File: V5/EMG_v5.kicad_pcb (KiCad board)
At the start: 2 copper layers, 75.2 x 32 mm, 20 parts, among them J1 SJ1-3523N, J2 Output, U1 INA333xxDGK, U2 MCP6002-xP

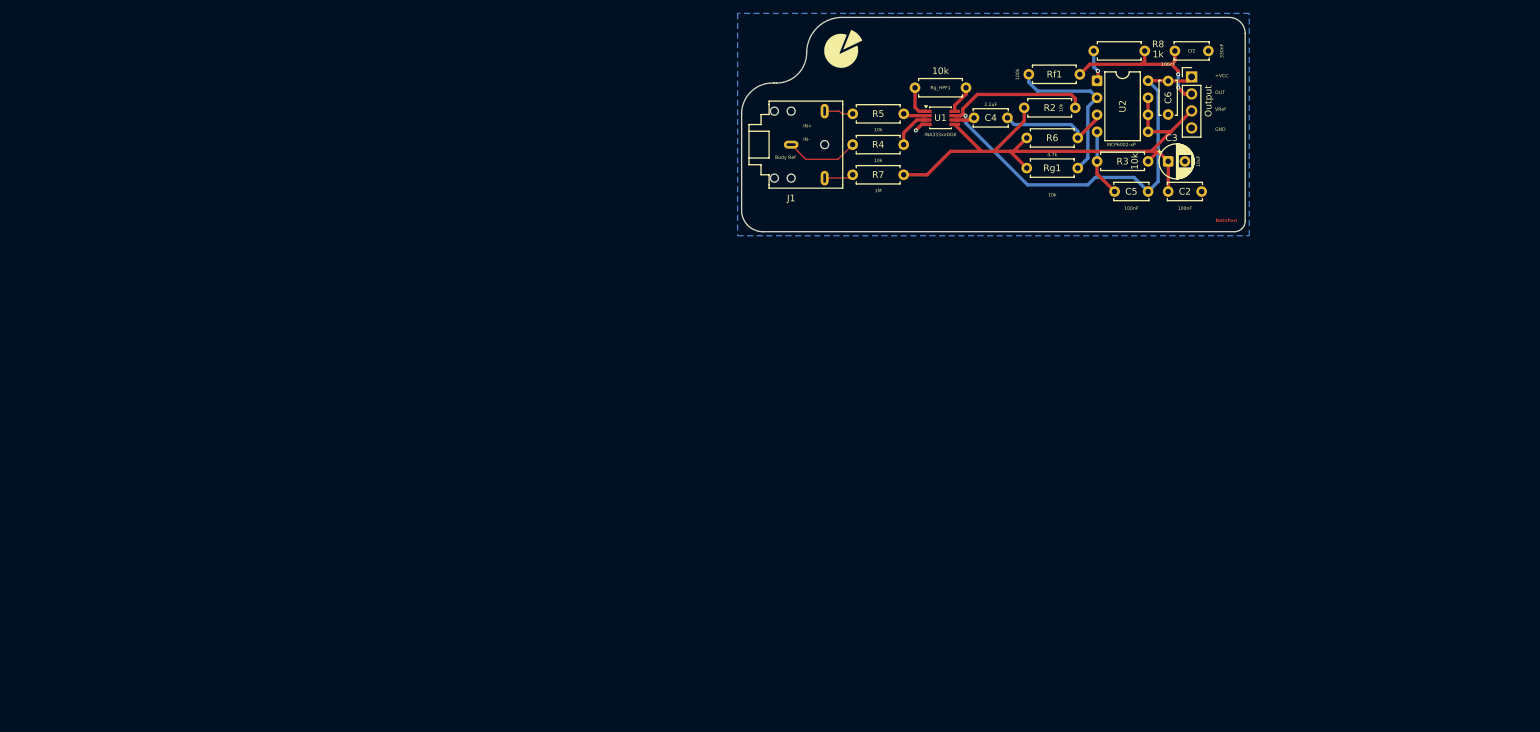
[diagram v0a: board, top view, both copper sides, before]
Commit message: Place EMG V5 PCB blocks and fix analog feedback nets
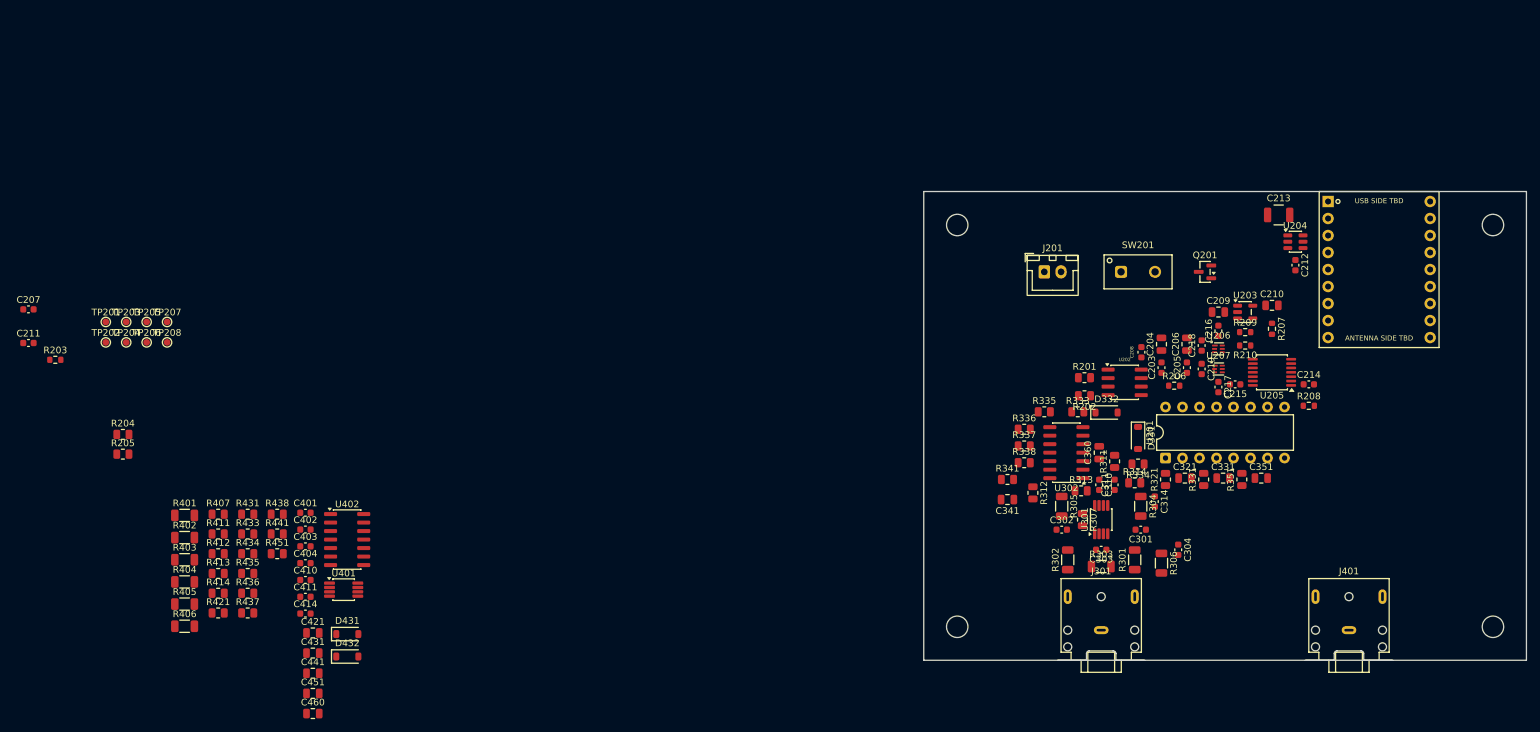
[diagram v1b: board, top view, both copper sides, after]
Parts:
- removed C2, C5, C6: 100nF, Capacitor_THT:C_Disc_D5.0mm_W2.5mm_P5.00mm
- removed C3: 10uF, Capacitor_THT:CP_Radial_D5.0mm_P2.50mm
- removed C4: 2.2uF, Capacitor_THT:C_Disc_D5.0mm_W2.5mm_P5.00mm
- removed Cf2: 330nF, Capacitor_THT:C_Disc_D5.0mm_W2.5mm_P5.00mm
- removed J1: SJ1-3523N, Connector_Audio:Jack_3.5mm_CUI_SJ1-3523N_Horizontal
- removed J2: Output, Connector_PinHeader_2.54mm:PinHeader_1x04_P2.54mm_Vertical
- removed R2, R3, R4, R5, Rg1, Rg_HPF1: 10k, Resistor_THT:R_Axial_DIN0207_L6.3mm_D2.5mm_P7.62mm_Horizontal
- removed R6: 4.7k, Resistor_THT:R_Axial_DIN0207_L6.3mm_D2.5mm_P7.62mm_Horizontal
- removed R7: 1M, Resistor_THT:R_Axial_DIN0207_L6.3mm_D2.5mm_P7.62mm_Horizontal
- removed R8: 1k, Resistor_THT:R_Axial_DIN0207_L6.3mm_D2.5mm_P7.62mm_Horizontal
- removed Rf1: 100k, Resistor_THT:R_Axial_DIN0207_L6.3mm_D2.5mm_P7.62mm_Horizontal
- removed U1: INA333xxDGK, Package_SO:VSSOP-8_3x3mm_P0.65mm
- removed U2: MCP6002-xP, Package_DIP:DIP-8_W7.62mm
- added C203: 100nF, Capacitor_SMD:C_0603_1608Metric, F.Cu at (75.5, 66.3)
- added C204: 1uF, Capacitor_SMD:C_0805_2012Metric, F.Cu at (75.5, 62.8)
- added C205: 100nF, Capacitor_SMD:C_0603_1608Metric, F.Cu at (79.3, 66.3)
- added C206: 1uF, Capacitor_SMD:C_0805_2012Metric, F.Cu at (79.3, 62.8)
- added C207: 220pF, Capacitor_SMD:C_0603_1608Metric, F.Cu at (-93.7, 57.6)
- added C208: 100nF, Capacitor_SMD:C_0603_1608Metric, F.Cu at (72.5, 64.0)
- added C209: 2.2uF, Capacitor_SMD:C_0805_2012Metric, F.Cu at (84.0, 58.0)
- added C210: 2.2uF, Capacitor_SMD:C_0805_2012Metric, F.Cu at (92.0, 57.0)
- added C211: 10nF, Capacitor_SMD:C_0603_1608Metric, F.Cu at (-93.7, 62.6)
- added C212: 2.2nF, Capacitor_SMD:C_0603_1608Metric, F.Cu at (95.5, 51.0)
- added C213: 47uF, EMG_V5:C_1210_3225_Murata_GRM32_Reflow, F.Cu at (93.0, 43.5)
- added C214: 100nF, Capacitor_SMD:C_0603_1608Metric, F.Cu at (97.5, 68.8)
- added C215: 100nF, Capacitor_SMD:C_0603_1608Metric, F.Cu at (86.5, 68.8)
- added C216: 100nF, Capacitor_SMD:C_0603_1608Metric, F.Cu at (84.0, 60.8)
- added C217: 100nF, Capacitor_SMD:C_0603_1608Metric, F.Cu at (84.0, 69.2)
- added C218: 9.1nF, Capacitor_SMD:C_0603_1608Metric, F.Cu at (81.5, 63.0)
- added C219: 9.1nF, Capacitor_SMD:C_0603_1608Metric, F.Cu at (81.5, 66.5)
- added C301: 100pF, Capacitor_SMD:C_0603_1608Metric, F.Cu at (72.4, 90.5)
- added C302: 100pF, Capacitor_SMD:C_0603_1608Metric, F.Cu at (60.6, 90.5)
- added C303: 470pF, Capacitor_SMD:C_0603_1608Metric, F.Cu at (66.5, 93.5)
- added C304: 100pF DNP, Capacitor_SMD:C_0603_1608Metric, F.Cu at (78.0, 93.5)
- added C310: 100nF, Capacitor_SMD:C_0603_1608Metric, F.Cu at (66.2, 83.8)
- added C311: 100nF, Capacitor_SMD:C_0603_1608Metric, F.Cu at (68.5, 83.8)
- added C314: 10nF, Capacitor_SMD:C_0603_1608Metric, F.Cu at (74.5, 86.3)
- added C321: 1nF, Capacitor_SMD:C_0805_2012Metric, F.Cu at (79.0, 82.8)
- added C331: 1nF, Capacitor_SMD:C_0805_2012Metric, F.Cu at (84.7, 82.8)
- added C341: 1uF, Capacitor_SMD:C_0805_2012Metric, F.Cu at (52.5, 86.0)
- added C351: 4.7nF, Capacitor_SMD:C_0805_2012Metric, F.Cu at (90.4, 82.8)
- added C360: 100nF, Capacitor_SMD:C_0805_2012Metric, F.Cu at (66.2, 79.0)
- added C401: 100pF, Capacitor_SMD:C_0603_1608Metric, F.Cu at (-52.3, 88.0)
- added C402: 100pF, Capacitor_SMD:C_0603_1608Metric, F.Cu at (-52.3, 90.5)
- added C403: 470pF, Capacitor_SMD:C_0603_1608Metric, F.Cu at (-52.3, 93.0)
- added C404: 100pF DNP, Capacitor_SMD:C_0603_1608Metric, F.Cu at (-52.3, 95.5)
- added C410: 100nF, Capacitor_SMD:C_0603_1608Metric, F.Cu at (-52.3, 98.0)
- added C411: 100nF, Capacitor_SMD:C_0603_1608Metric, F.Cu at (-52.3, 100.5)
- added C414: 10nF, Capacitor_SMD:C_0603_1608Metric, F.Cu at (-52.3, 103.0)
- added C421: 1nF, Capacitor_SMD:C_0805_2012Metric, F.Cu at (-51.2, 105.9)
- added C431: 1nF, Capacitor_SMD:C_0805_2012Metric, F.Cu at (-51.2, 108.9)
- added C441: 1uF, Capacitor_SMD:C_0805_2012Metric, F.Cu at (-51.2, 111.9)
- added C451: 4.7nF, Capacitor_SMD:C_0805_2012Metric, F.Cu at (-51.2, 115.0)
- added C460: 100nF, Capacitor_SMD:C_0805_2012Metric, F.Cu at (-51.2, 118.0)
- added D331: BAS70ZFILM, Diode_SMD:D_SOD-123, F.Cu at (72.0, 76.8)
- added D332: BAS70ZFILM, Diode_SMD:D_SOD-123, F.Cu at (67.3, 73.0)
- added D431: BAS70ZFILM, Diode_SMD:D_SOD-123, F.Cu at (-46.1, 106.1)
- added D432: BAS70ZFILM, Diode_SMD:D_SOD-123, F.Cu at (-46.1, 109.4)
- added J201: B2B-XH-A(LF)(SN), Connector_JST:JST_XH_B2B-XH-A_1x02_P2.50mm_Vertical, F.Cu at (58.0, 52.0)
- added J301: SJ1-3523N, Connector_Audio:Jack_3.5mm_CUI_SJ1-3523N_Horizontal, F.Cu at (66.5, 105.5)
- added J401: SJ1-3523N, Connector_Audio:Jack_3.5mm_CUI_SJ1-3523N_Horizontal, F.Cu at (103.5, 105.5)
- added Q201: PMV48XP, Package_TO_SOT_SMD:SOT-23, F.Cu at (82.0, 52.0)
- added R201: 47k, Resistor_SMD:R_0805_2012Metric, F.Cu at (64.0, 67.8)
- added R202: 47k, Resistor_SMD:R_0805_2012Metric, F.Cu at (64.0, 70.5)
- added R203: 1k, Resistor_SMD:R_0603_1608Metric, F.Cu at (-89.7, 65.1)
- added R204: 68k, Resistor_SMD:R_0805_2012Metric, F.Cu at (-79.6, 76.3)
- added R205: 100k, Resistor_SMD:R_0805_2012Metric, F.Cu at (-79.6, 79.2)
- added R206: 0R, Resistor_SMD:R_0603_1608Metric, F.Cu at (77.4, 69.0)
- added R207: 0R, Resistor_SMD:R_0603_1608Metric, F.Cu at (92.0, 60.5)
- added R208: 10k, Resistor_SMD:R_0603_1608Metric, F.Cu at (97.5, 72.0)
- added R209: 47k 1%, Resistor_SMD:R_0603_1608Metric, F.Cu at (88.0, 61.0)
- added R210: 220k 1%, Resistor_SMD:R_0603_1608Metric, F.Cu at (88.0, 63.0)
- added R301: 100k, Resistor_SMD:R_1206_3216Metric, F.Cu at (71.5, 95.0)
- added R302: 100k, Resistor_SMD:R_1206_3216Metric, F.Cu at (61.5, 95.0)
- added R303: 220k, Resistor_SMD:R_1206_3216Metric, F.Cu at (66.5, 96.0)
- added R304: 10M, Resistor_SMD:R_1206_3216Metric, F.Cu at (72.4, 87.0)
- added R305: 10M, Resistor_SMD:R_1206_3216Metric, F.Cu at (60.6, 87.0)
- added R306: 2.2M, Resistor_SMD:R_1206_3216Metric, F.Cu at (75.5, 95.5)
- added R307: 4.99k 0.1% RG, Resistor_SMD:R_0805_2012Metric, F.Cu at (63.7, 89.0)
- added R311: 100k, Resistor_SMD:R_0805_2012Metric, F.Cu at (68.5, 80.3)
- added R312: 10k, Resistor_SMD:R_0805_2012Metric, F.Cu at (56.3, 85.0)
- added R313: 40.2k, Resistor_SMD:R_0805_2012Metric, F.Cu at (63.5, 84.7)
- added R314: 33k, Resistor_SMD:R_0805_2012Metric, F.Cu at (71.5, 83.5)
- added R321: 470R, Resistor_SMD:R_0805_2012Metric, F.Cu at (76.1, 83.0)
- added R331: 470R, Resistor_SMD:R_0805_2012Metric, F.Cu at (81.8, 83.0)
- added R333: 10k, Resistor_SMD:R_0805_2012Metric, F.Cu at (63.0, 72.9)
- added R334: 10k, Resistor_SMD:R_0805_2012Metric, F.Cu at (72.0, 80.7)
- added R335: 1M, Resistor_SMD:R_0805_2012Metric, F.Cu at (58.0, 72.9)
- added R336: 20k, Resistor_SMD:R_0805_2012Metric, F.Cu at (55.0, 75.5)
- added R337: 10k, Resistor_SMD:R_0805_2012Metric, F.Cu at (55.0, 78.0)
- added R338: 20k, Resistor_SMD:R_0805_2012Metric, F.Cu at (55.0, 80.5)
- added R341: 33k, Resistor_SMD:R_0805_2012Metric, F.Cu at (52.5, 83.0)
- added R351: 470R, Resistor_SMD:R_0805_2012Metric, F.Cu at (87.5, 83.0)
- added R401: 100k, Resistor_SMD:R_1206_3216Metric, F.Cu at (-70.4, 88.4)
- added R402: 100k, Resistor_SMD:R_1206_3216Metric, F.Cu at (-70.4, 91.7)
- added R403: 220k, Resistor_SMD:R_1206_3216Metric, F.Cu at (-70.4, 95.0)
- added R404: 10M, Resistor_SMD:R_1206_3216Metric, F.Cu at (-70.4, 98.3)
- added R405: 10M, Resistor_SMD:R_1206_3216Metric, F.Cu at (-70.4, 101.6)
- added R406: 2.2M, Resistor_SMD:R_1206_3216Metric, F.Cu at (-70.4, 104.9)
- added R407: 4.99k 0.1% RG, Resistor_SMD:R_0805_2012Metric, F.Cu at (-65.4, 88.2)
- added R411: 100k, Resistor_SMD:R_0805_2012Metric, F.Cu at (-65.4, 91.1)
- added R412: 10k, Resistor_SMD:R_0805_2012Metric, F.Cu at (-65.4, 94.1)
- added R413: 40.2k, Resistor_SMD:R_0805_2012Metric, F.Cu at (-65.4, 97.0)
- added R414: 33k, Resistor_SMD:R_0805_2012Metric, F.Cu at (-65.4, 100.0)
- added R421: 470R, Resistor_SMD:R_0805_2012Metric, F.Cu at (-65.4, 102.9)
- added R431: 470R, Resistor_SMD:R_0805_2012Metric, F.Cu at (-61.0, 88.2)
- added R433: 10k, Resistor_SMD:R_0805_2012Metric, F.Cu at (-61.0, 91.1)
- added R434: 10k, Resistor_SMD:R_0805_2012Metric, F.Cu at (-61.0, 94.1)
- added R435: 1M, Resistor_SMD:R_0805_2012Metric, F.Cu at (-61.0, 97.0)
- added R436: 20k, Resistor_SMD:R_0805_2012Metric, F.Cu at (-61.0, 100.0)
- added R437: 10k, Resistor_SMD:R_0805_2012Metric, F.Cu at (-61.0, 102.9)
- added R438: 20k, Resistor_SMD:R_0805_2012Metric, F.Cu at (-56.5, 88.2)
- added R441: 33k, Resistor_SMD:R_0805_2012Metric, F.Cu at (-56.5, 91.1)
- added R451: 470R, Resistor_SMD:R_0805_2012Metric, F.Cu at (-56.5, 94.1)
- added REF**: MountingHole_3.2mm_M3, MountingHole:MountingHole_3.2mm_M3, F.Cu at (125.0, 105.0)
- added REF**: MountingHole_3.2mm_M3, MountingHole:MountingHole_3.2mm_M3, F.Cu at (125.0, 45.0)
- added REF**: MountingHole_3.2mm_M3, MountingHole:MountingHole_3.2mm_M3, F.Cu at (45.0, 105.0)
- added REF**: MountingHole_3.2mm_M3, MountingHole:MountingHole_3.2mm_M3, F.Cu at (45.0, 45.0)
- added SW201: TS02CQE, EMG_V5:TS02CQE_SPST_THT, F.Cu at (72.0, 52.0)
- added TP201: BAT_PACK+, TestPoint:TestPoint_Pad_D1.0mm, F.Cu at (-82.2, 59.5)
- added TP202: SW_BAT+, TestPoint:TestPoint_Pad_D1.0mm, F.Cu at (-82.2, 62.5)
- added TP203: LDO_IN, TestPoint:TestPoint_Pad_D1.0mm, F.Cu at (-79.1, 59.5)
- added TP204: 3V3_ADC, TestPoint:TestPoint_Pad_D1.0mm, F.Cu at (-79.1, 62.5)
- added TP205: BAT_MON, TestPoint:TestPoint_Pad_D1.0mm, F.Cu at (-76.0, 59.5)
- added TP206: GND, TestPoint:TestPoint_Pad_D1.0mm, F.Cu at (-76.0, 62.5)
- added TP207: CARRIER_3V3, TestPoint:TestPoint_Pad_D1.0mm, F.Cu at (-73.0, 59.5)
- added TP208: SPI_ISO_OE, TestPoint:TestPoint_Pad_D1.0mm, F.Cu at (-73.0, 62.5)
- added U201: MCP3208-CI/P, Package_DIP:DIP-16_W7.62mm, F.Cu at (76.1, 79.8)
- added U202: MCP6002-I/SN, Package_SO:SOIC-8_3.9x4.9mm_P1.27mm, F.Cu at (70.0, 68.5)
- added U203: TPS7A2033PDBVR, Package_TO_SOT_SMD:SOT-23-5, F.Cu at (88.0, 58.0)
- added U204: TPS22917DBVR, Package_TO_SOT_SMD:SOT-23-6, F.Cu at (95.5, 47.5)
- added U205: TXU0304PWR, Package_SO:TSSOP-14_4.4x5mm_P0.65mm, F.Cu at (92.0, 67.0)
- added U206: TPS3899DL30DSER, Package_SON:WSON-6_1.5x1.5mm_P0.5mm, F.Cu at (84.0, 63.5)
- added U207: TPS3899DL29DSER, Package_SON:WSON-6_1.5x1.5mm_P0.5mm, F.Cu at (84.0, 66.5)
- added U301: INA333AIDGKT, Package_SO:VSSOP-8_3x3mm_P0.65mm, F.Cu at (66.5, 89.0)
- added U302: MCP6004-I/SL, Package_SO:SOIC-14_3.9x8.7mm_P1.27mm, F.Cu at (61.3, 79.0)
- added U401: INA333AIDGKT, Package_SO:VSSOP-8_3x3mm_P0.65mm, F.Cu at (-46.6, 99.5)
- added U402: MCP6004-I/SL, Package_SO:SOIC-14_3.9x8.7mm_P1.27mm, F.Cu at (-46.1, 92.0)
- added U501: DSTK22807_ESP32H2_SuperMini_Measured, EMG_V5:DSTK22807_ESP32H2_SuperMini_Carrier_Measured_THT, F.Cu at (108.0, 51.6)
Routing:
- net /VREF: track 85.6 -> 0.00 mm
- net VCC: track 80.0 -> 0.00 mm, vias 1 -> 0
- net /RAW_Out: track 25.0 -> 0.00 mm, vias 2 -> 0
- net Net-(U2A--): track 24.0 -> 0.00 mm
- net /HPF_Out: track 17.0 -> 0.00 mm
- net GND: track 12.0 -> 0.00 mm, vias 1 -> 0
- net /IN+: track 11.0 -> 0.00 mm
- net Net-(U1-+): track 5.93 -> 0.00 mm
- net Net-(Rg_HPF1-Pad1): track 4.88 -> 0.00 mm
- net Net-(R8-Pad1): track 4.77 -> 0.00 mm, vias 1 -> 0
- net /BODY_REF: track 4.39 -> 0.00 mm
- net /IN-: track 4.36 -> 0.00 mm
- net Net-(Rg_HPF1-Pad2): track 4.23 -> 0.00 mm
- net Net-(U1--): track 3.46 -> 0.00 mm
- net /INA_OUT: track 3.06 -> 0.00 mm
- removed copper zone on B.Cu, net GND
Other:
- board size 75.2 x 32 mm -> 90 x 70 mm
- board text added: "EMG_Batuhxn"
- board text removed: "+VCC"
- board text removed: "Batuhxn"
- board text removed: "Body Ref"
- board text removed: "GND"
- board text removed: "IN+"
- board text removed: "IN-"
- board text removed: "OUT"
- board text removed: "VRef"

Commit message: Complete V5 PCB placement and debug access
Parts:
- added SW501: DEBUG_CFG, Button_Switch_THT:SW_DIP_SPSTx04_Slide_9.78x12.34mm_W7.62mm_P2.54mm, F.Cu at (46.5, 59.0)
- added TP301: EMG1_IA_OUT, TestPoint:TestPoint_Pad_D1.5mm, F.Cu at (69.7, 87.0)
- added TP302: EMG1_RAW_DRV, TestPoint:TestPoint_Pad_D1.5mm, F.Cu at (48.5, 75.5)
- added TP303: EMG1_RECT_DRV, TestPoint:TestPoint_Pad_D1.5mm, F.Cu at (48.5, 80.8)
- added TP304: EMG1_ENV_DRV, TestPoint:TestPoint_Pad_D1.5mm, F.Cu at (48.5, 91.0)
- added TP305: GND_CH1, TestPoint:TestPoint_Pad_D2.0mm, F.Cu at (77.0, 102.5)
- added TP306: ANALOG_VREF, TestPoint:TestPoint_Pad_D1.5mm, F.Cu at (48.5, 86.0)
- added TP401: EMG2_IA_OUT, TestPoint:TestPoint_Pad_D1.5mm, F.Cu at (106.8, 86.8)
- added TP402: EMG2_RAW_DRV, TestPoint:TestPoint_Pad_D1.5mm, F.Cu at (85.8, 93.8)
- added TP403: EMG2_RECT_DRV, TestPoint:TestPoint_Pad_D1.5mm, F.Cu at (102.5, 68.8)
- added TP404: EMG2_ENV_DRV, TestPoint:TestPoint_Pad_D1.5mm, F.Cu at (85.8, 99.0)
- added TP405: GND_CH2, TestPoint:TestPoint_Pad_D2.0mm, F.Cu at (113.8, 102.5)
- moved TP206 196.3 mm to (120.0, 53.0)
- moved TP207 193.2 mm to (120.0, 50.0)
- moved C211 184.4 mm to (85.5, 106.0)
- moved R406 183.1 mm to (112.5, 95.5), turned to -90 degrees
- moved R404 180.1 mm to (109.4, 87.0), turned to -90 degrees
- moved R414 179.6 mm to (113.5, 83.3)
- moved R401 179.0 mm to (108.5, 95.0), turned to 90 degrees
- moved C207 178.3 mm to (81.8, 89.2), turned to -90 degrees
- moved R413 175.4 mm to (109.5, 83.3)
- moved TP204 175.2 mm to (96.0, 57.0)
- moved R412 173.9 mm to (108.0, 80.3), turned to 90 degrees
- moved R403 173.9 mm to (103.5, 96.0)
- moved R203 172.8 mm to (81.8, 86.5)
- moved R435 172.2 mm to (109.3, 71.4), turned to 180 degrees
- moved R411 171.2 mm to (105.5, 80.3), turned to 90 degrees
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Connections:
- net /GND renamed GND
- U501 pad 17: unconnected-(U501-GPIO10-Pad17) -> /CFG_CAL
- U501 pad 3: unconnected-(U501-GPIO0-Pad3) -> /CFG_SERVICE
- U501 pad 4: unconnected-(U501-GPIO1-Pad4) -> /CFG_LED
- U501 pad 8: unconnected-(U501-GPIO5-Pad8) -> /CFG_FILTER
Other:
- outline, holes or cut-outs redrawn

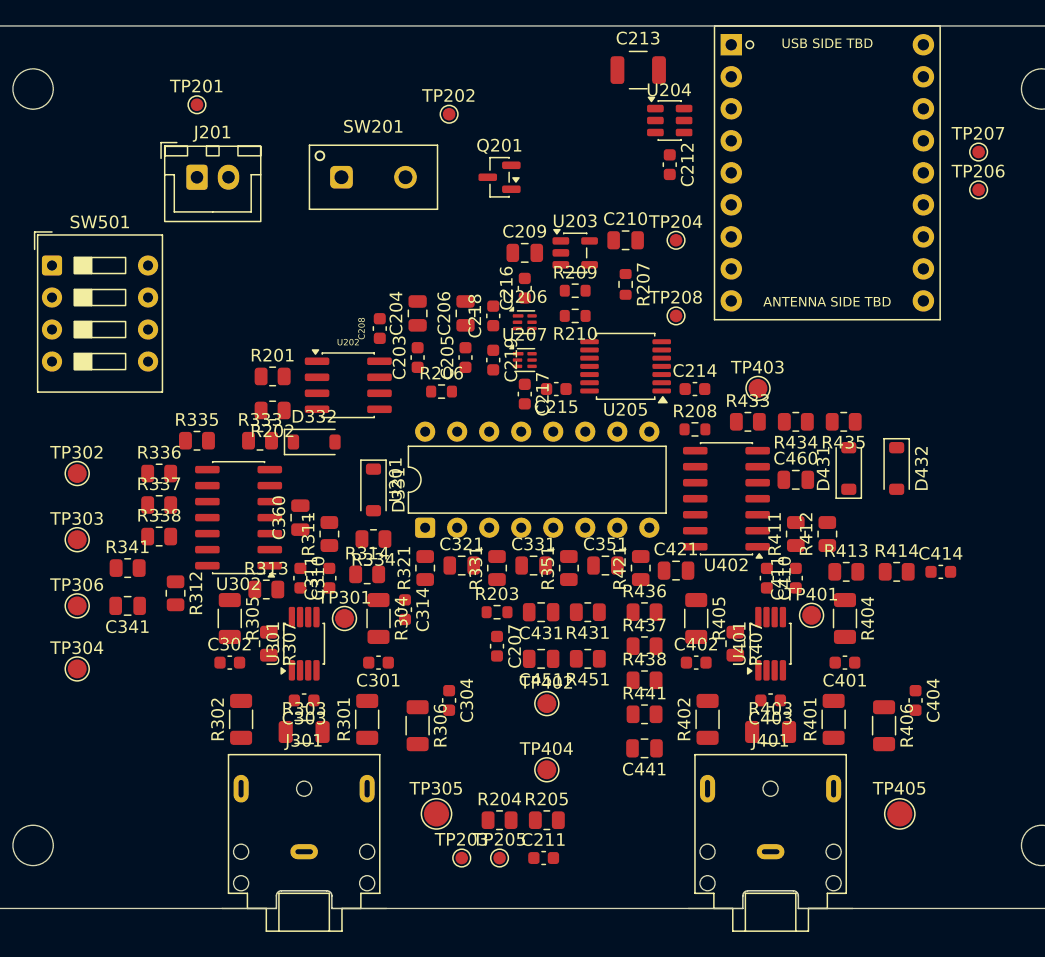
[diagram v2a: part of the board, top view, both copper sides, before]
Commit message: Update V5 routing and INA333 footprint
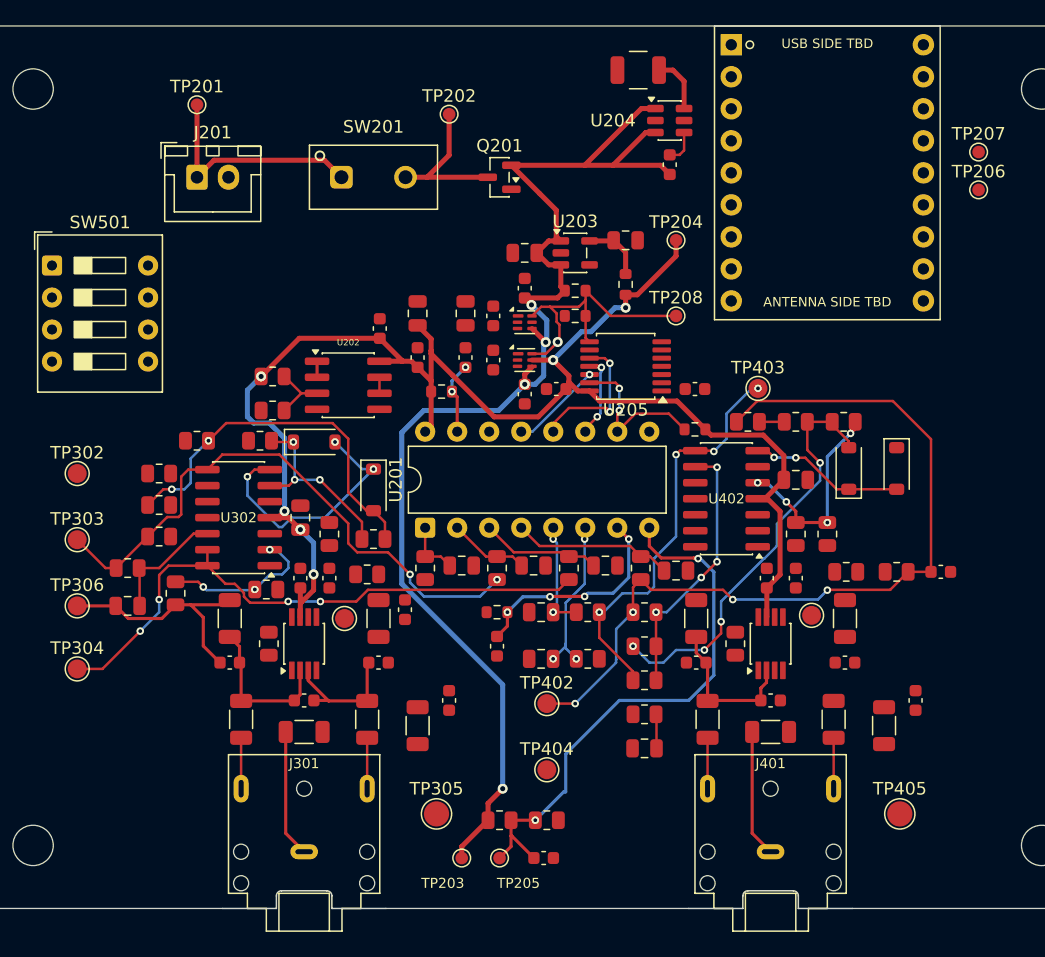
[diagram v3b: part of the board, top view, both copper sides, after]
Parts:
- U301, U401: footprint Package_SO:VSSOP-8_3x3mm_P0.65mm -> EMG_V5:INA333_DGK_VSSOP-8_TI
- turned C209 to 180 degrees
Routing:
- net /EMG_CHANNEL_1_ANALOG/3V3_ADC: track 0.00 -> 122.0 mm, vias 0 -> 6
- net /POWER_REFERENCE_BLOCK/LDO_IN: track 0.00 -> 104.3 mm, vias 0 -> 4
- net /EMG_CHANNEL_2_ANALOG/EMG2_RAW_DRV: track 0.00 -> 66.7 mm, vias 0 -> 4
- net /EMG_CHANNEL_1_ANALOG/EMG1_ENV_DRV: track 0.00 -> 47.6 mm, vias 0 -> 4
- net /EMG_CHANNEL_1_ANALOG/EMG1_RECT_DRV: track 0.00 -> 46.2 mm, vias 0 -> 2
- net /POWER_REFERENCE_BLOCK/BAT_MON: track 0.00 -> 44.1 mm, vias 0 -> 2
- net /EMG_CHANNEL_1_ANALOG/analog VREF: track 0.00 -> 36.2 mm, vias 0 -> 4
- net /EMG_CHANNEL_2_ANALOG/EMG2_RECT_A1_OUT: track 0.00 -> 33.5 mm, vias 0 -> 4
- net /EMG_CHANNEL_2_ANALOG/EMG2_RECT_DRV: track 0.00 -> 32.8 mm, vias 0 -> 4
- net /EMG_CHANNEL_1_ANALOG/EMG1_RECT_A1_OUT: track 0.00 -> 29.7 mm, vias 0 -> 2
- net /POWER_REFERENCE_BLOCK/SPI_ISO_OE: track 0.00 -> 22.5 mm, vias 0 -> 1
- net /EMG_CHANNEL_2_ANALOG/EMG2_RECT_SUM2: track 0.00 -> 21.1 mm, vias 0 -> 4
- net /EMG_CHANNEL_1_ANALOG/EMG1_RECT_U302B_DRV: track 0.00 -> 20.4 mm, vias 0 -> 3
- net /POWER_REFERENCE_BLOCK/BAT_PACK+: track 0.00 -> 18.3 mm
- net /POWER_REFERENCE_BLOCK/VREF_MON: track 0.00 -> 17.4 mm, vias 0 -> 4
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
